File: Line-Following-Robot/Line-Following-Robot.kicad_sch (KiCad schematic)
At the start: 10 parts, among them SW1 SW_Push, SW2 SW_Push, U1 LM317LZ

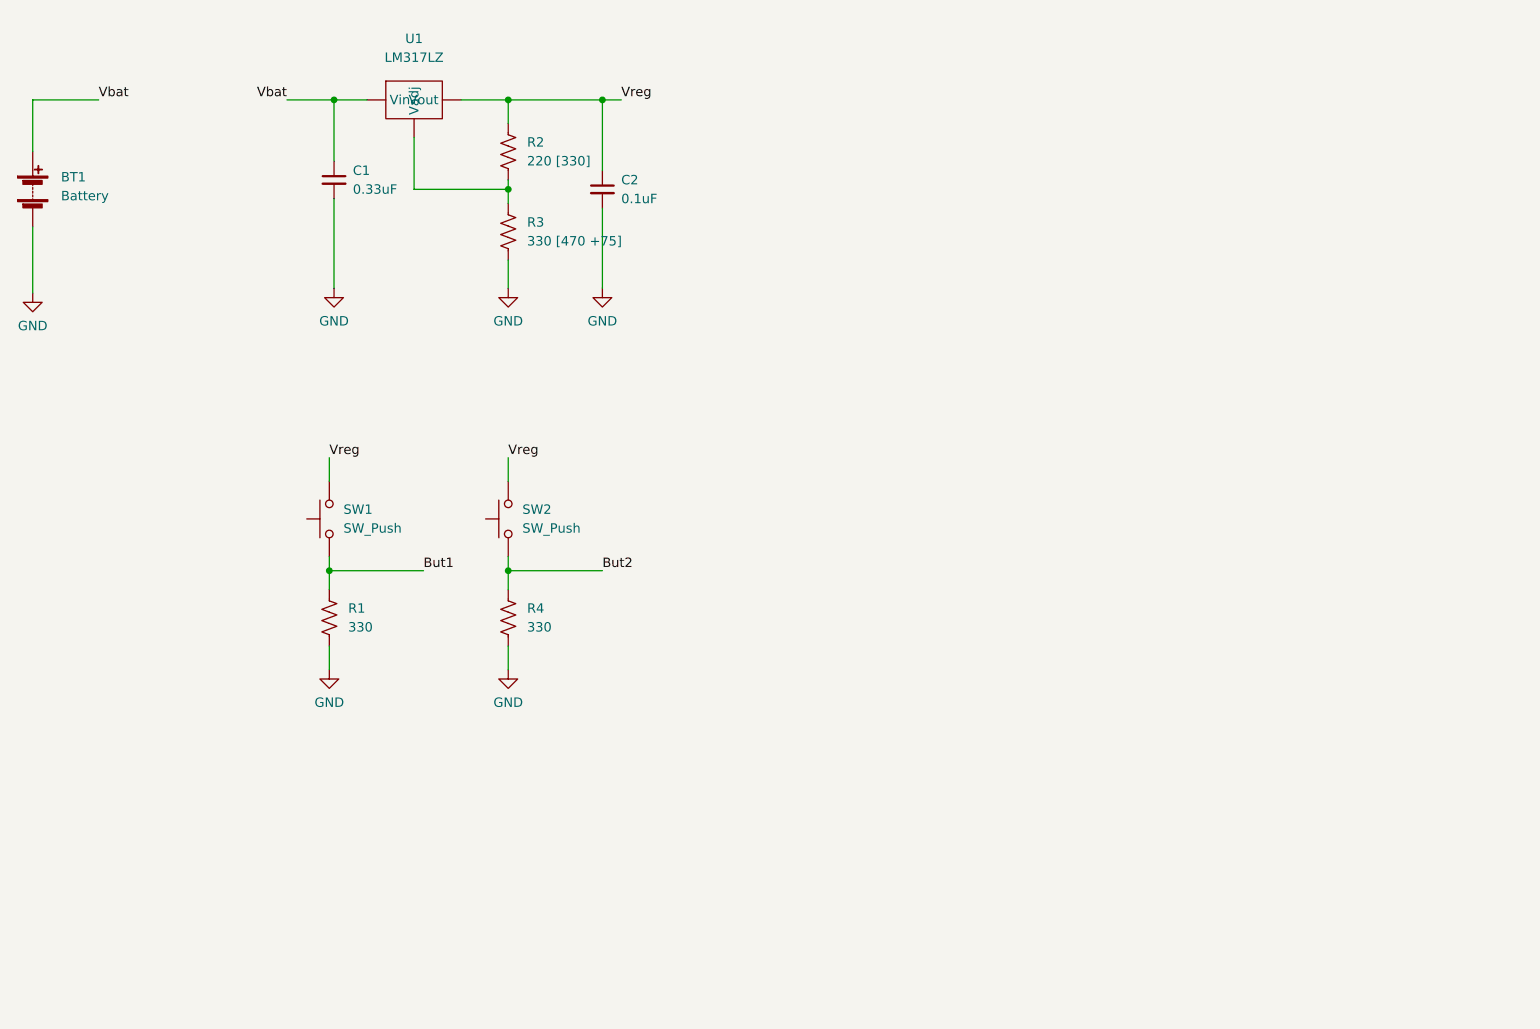
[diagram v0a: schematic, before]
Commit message: Schematic for light detection done
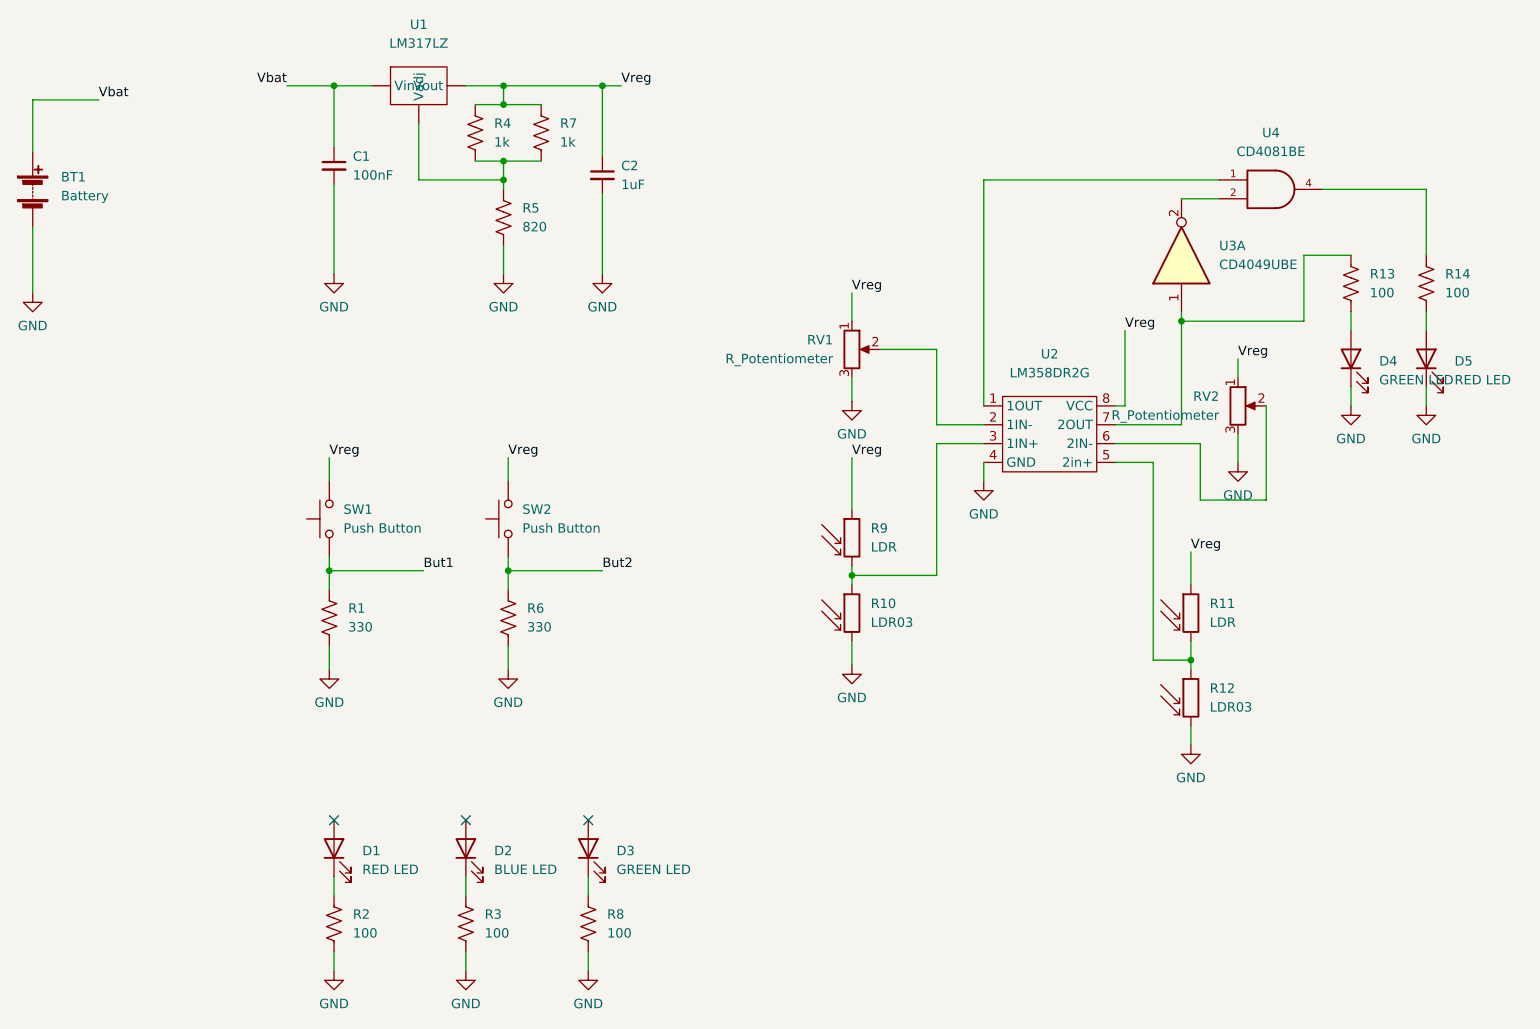
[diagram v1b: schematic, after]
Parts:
- added D1, D5: RED LED, symbol Device:LED
- added D2: BLUE LED, symbol Device:LED
- added D3, D4: GREEN LED, symbol Device:LED
- added R10, R12: LDR03, OptoDevice:R_LDR_10x8.5mm_P7.6mm_Vertical, symbol Sensor_Optical:LDR03
- added R11, R9: LDR, OptoDevice:R_LDR_10x8.5mm_P7.6mm_Vertical, symbol Sensor_Optical:LDR03
- added R13, R14, R2, R3, R8: 100, symbol Device:R_US
- added R7: 1k, symbol Device:R_US
- added RV1, RV2: R_Potentiometer, symbol Device:R_Potentiometer
- added U2: LM358DR2G, symbol PCB_Library_From_Template:LM358DR2G
- added U3: CD4049UBE, symbol 74xx:74LS04
- added U4: CD4081BE, symbol 74xGxx:74AHC1G08
- C1: value 0.33uF -> 100nF; Required (none) -> YES
- C2: value 0.1uF -> 1uF; Required (none) -> YES
- R1, U1: Required (none) -> YES
- R4: renamed from R2; value 220 [330] -> 1k; Required (none) -> YES
- R5: renamed from R3; value 330 [470 +75] -> 820; Required (none) -> YES
- R6: renamed from R4; Required (none) -> YES
- SW1, SW2: value SW_Push -> Push Button; Required (none) -> YES
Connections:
- net GND: now also D4.1 (K), D5.1 (K), R10.2, R12.2, R2.2, R3.2, R8.2, RV1.3, RV2.3, U2.4 (GND), U4.3 (GND)
- net Vreg: now also R11.1, R7.1, R9.1, RV1.1, RV2.1, U2.8 (VCC)
- net at R4.2, R5.1, U1. (Vout): now also R7.2
- new net: D3.1 (K), R8.1
- new net: U2.1 (1OUT), U4.1
- new net: RV1.2, U2.2 (1IN-)
- new net: R10.1, R9.2, U2.3 (1IN+)
- new net: R11.2, R12.1, U2.5 (2in+)
- new net: RV2.2, U2.6 (2IN-)
- new net: R13.1, U2.7 (2OUT), U3.1
- new net: U3.2, U4.2
- new net: D4.2 (A), R13.2
- new net: D1.1 (K), R2.1
- new net: R14.1, U4.4
- new net: D5.2 (A), R14.2
- new net: D2.1 (K), R3.1
- new net VCC: U4.5 (VCC)
- no-connect marks 0 -> 3
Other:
- moved on the sheet: C1, C2, R4, R5, U1

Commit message: Updated schematic and BOM
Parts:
- R1, R6: value 330 -> 10k
- U3: value CD4049UBE -> CD4011BE
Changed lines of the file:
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@@
       (effects (font (size 1.27 1.27)) (justify right))
     )
-    (property "Value" "CD4049UBE" (id 1) (at 181.61 50.7999 90)
+    (property "Value" "CD4011BE" (id 1) (at 181.61 50.7999 90)
       (effects (font (size 1.27 1.27)) (justify right))
     )
@@
       (effects (font (size 1.27 1.27)) (justify left))
     )
-    (property "Value" "330" (id 1) (at 88.265 99.6949 0)
+    (property "Value" "10k" (id 1) (at 88.265 99.6949 0)
       (effects (font (size 1.27 1.27)) (justify left))
     )
@@
       (effects (font (size 1.27 1.27)) (justify left))
     )
-    (property "Value" "330" (id 1) (at 64.135 99.6949 0)
+    (property "Value" "10k" (id 1) (at 64.135 99.6949 0)
       (effects (font (size 1.27 1.27)) (justify left))
     )
@@
     )
     (path "/98ce9caf-5efc-4885-b55b-9201117aef6e"
-      (reference "R1") (unit 1) (value "330") (footprint "")
+      (reference "R1") (unit 1) (value "10k") (footprint "")
     )
     (path "/43064d00-084c-4e4c-8e6c-67264db5fdd4"
@@
     )
     (path "/762008aa-5574-4b5e-8d04-ab8d4b0b5299"
-      (reference "R6") (unit 1) (value "330") (footprint "")
+      (reference "R6") (unit 1) (value "10k") (footprint "")
     )
     (path "/1d81c3e7-f1f9-495c-a16f-d7987c13482d"
@@
     )
     (path "/20a52576-749e-438a-87ed-de267033f6a8"
-      (reference "U3") (unit 1) (value "CD4049UBE") (footprint "")
+      (reference "U3") (unit 1) (value "CD4011BE") (footprint "")
     )
     (path "/d26a0fc9-5b19-4dd5-84f8-8f657e2b2349"
